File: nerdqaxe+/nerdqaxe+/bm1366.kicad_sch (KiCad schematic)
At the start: 78 parts, among them J2 Conn_01x06, U19 BM1368_mode1, U20 BM1368_mode1, U25 BM1368_mode1, U26 BM1368_mode1, U35 TXU0304PW, U8 25MHz

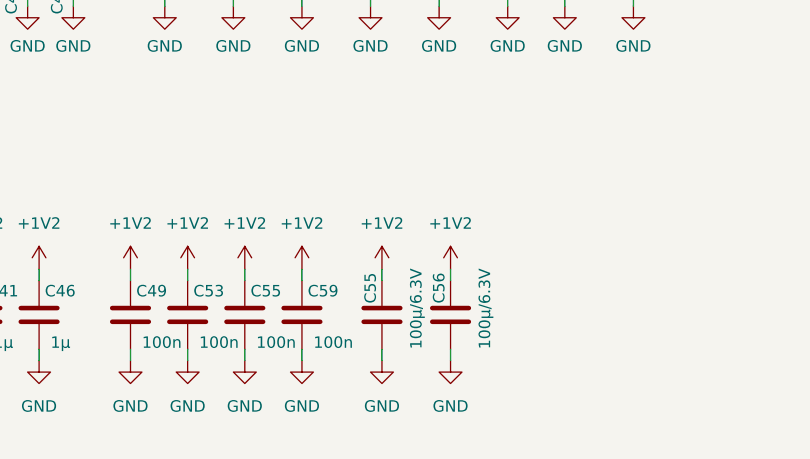
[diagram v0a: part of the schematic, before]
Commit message: updated bom of + for 24V cap
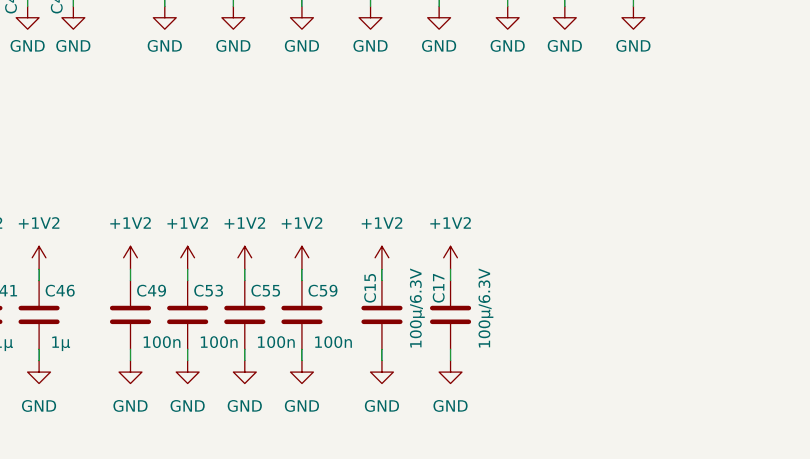
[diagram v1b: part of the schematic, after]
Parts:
- U35: footprint Package_SO:TSSOP-14_4.4x5mm_P0.65mm -> Package_SO:TSSOP-14_4.4x5mm_P0.65mm
- renumbered C55 to C15, C56 to C17
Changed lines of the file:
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@@
 (kicad_sch
-	(version 20231120)
+	(version 20250114)
 	(generator "eeschema")
-	(generator_version "8.0")
+	(generator_version "9.0")
 	(paper "A3")
 	(title_block
@@
 	(label "RO"
 		(at 337.82 55.88 180)
-		(fields_autoplaced yes)
 		(effects
 			(font
@@
 	(label "RESET"
 		(at 365.76 50.8 0)
-		(fields_autoplaced yes)
 		(effects
 			(font
@@
 	(label "RST_N"
 		(at 261.62 241.3 180)
-		(fields_autoplaced yes)
 		(effects
 			(font
@@
 	(label "RO"
 		(at 101.6 66.04 0)
-		(fields_autoplaced yes)
 		(effects
 			(font
@@
 	(label "CI"
 		(at 260.35 246.38 180)
-		(fields_autoplaced yes)
 		(effects
 			(font
@@
 	(label "CLKI"
 		(at 101.6 68.58 0)
-		(fields_autoplaced yes)
 		(effects
 			(font
@@
 	(label "TXD"
 		(at 30.48 44.45 0)
-		(fields_autoplaced yes)
 		(effects
 			(font
@@
 	(label "RXD"
 		(at 30.48 41.91 0)
-		(fields_autoplaced yes)
 		(effects
 			(font
@@
 	(label "RST_N"
 		(at 101.6 60.96 0)
-		(fields_autoplaced yes)
 		(effects
 			(font
@@
 	(label "TXD"
 		(at 365.76 48.26 0)
-		(fields_autoplaced yes)
 		(effects
 			(font
@@
 	(label "RST_N"
 		(at 337.82 50.8 180)
-		(fields_autoplaced yes)
 		(effects
 			(font
@@
 	(label "RXD"
 		(at 365.76 55.88 0)
-		(fields_autoplaced yes)
 		(effects
 			(font
@@
 	(label "RESET"
 		(at 30.48 46.99 0)
-		(fields_autoplaced yes)
 		(effects
 			(font
@@
 	(label "RO"
 		(at 261.62 243.84 180)
-		(fields_autoplaced yes)
 		(effects
 			(font
@@
 	(label "BI"
 		(at 101.6 71.12 0)
-		(fields_autoplaced yes)
 		(effects
 			(font
@@
 	(label "CI"
 		(at 101.6 63.5 0)
-		(fields_autoplaced yes)
 		(effects
 			(font
@@
 	(label "CI"
 		(at 337.82 48.26 180)
-		(fields_autoplaced yes)
 		(effects
 			(font
@@
 		(shape input)
 		(at 29.21 31.75 180)
-		(fields_autoplaced yes)
 		(effects
 			(font
@@
 		(shape input)
 		(at 29.21 39.37 180)
-		(fields_autoplaced yes)
 		(effects
 			(font
@@
 		(shape input)
 		(at 29.21 36.83 180)
-		(fields_autoplaced yes)
 		(effects
 			(font
@@
 		(shape output)
 		(at 29.21 44.45 180)
-		(fields_autoplaced yes)
 		(effects
 			(font
@@
 		(shape output)
 		(at 29.21 46.99 180)
-		(fields_autoplaced yes)
 		(effects
 			(font
@@
 		(shape input)
 		(at 29.21 34.29 180)
-		(fields_autoplaced yes)
 		(effects
 			(font
@@
 		(shape input)
 		(at 29.21 41.91 180)
-		(fields_autoplaced yes)
 		(effects
 			(font
@@
 			)
 		)
-		(property "Footprint" "Package_SO:TSSOP-14_4.4x5mm_P0.65mm "
+		(property "Footprint" "Package_SO:TSSOP-14_4.4x5mm_P0.65mm"
 			(at 360.68 48.26 0)
 			(effects
@@
 		(on_board yes)
 		(dnp no)
-		(property "Reference" "C55"
+		(property "Reference" "C15"
 			(at 137.16 241.3 90)
 			(effects
@@
 		(on_board yes)
 		(dnp no)
-		(property "Reference" "C56"
+		(property "Reference" "C17"
 			(at 144.78 241.3 90)
 			(effects
